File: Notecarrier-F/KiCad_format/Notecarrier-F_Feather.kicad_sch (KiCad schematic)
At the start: 13 parts, among them J7 SM04B-SRSS-TB(LF)(SN), J8 SM04B-SRSS-TB(LF)(SN), SW3 PTS810 SJM 250 SMTR LFS, SW4 CJS-1200TA, SW5 CJS-1200TA, U4 TXS0102DCUR, U6 DGQ2788AEN-T1-GE4

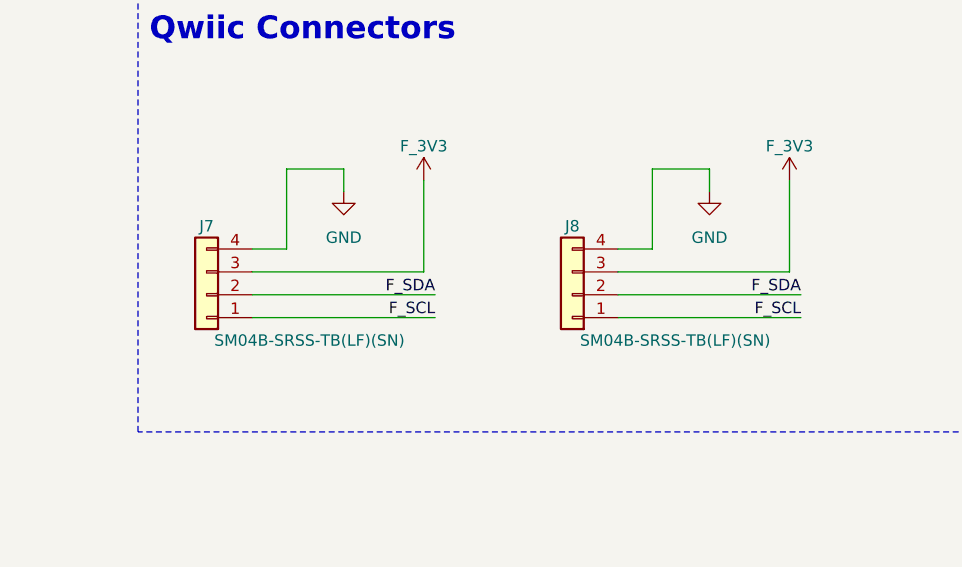
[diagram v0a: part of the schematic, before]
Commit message: Back fill symbol for SM04B-SRSS-TB / BM04B-SRSS-TBT.
Symbol created in the process of porting Notecarrier-A. Creating the symbol wasn’t justified when porting -B and -F, now it exists it’s best to be consistent even though these are SM04B-SRSS-TB (side entry) and the symbol was created for BM04B-SRSS-TBT (top entry).
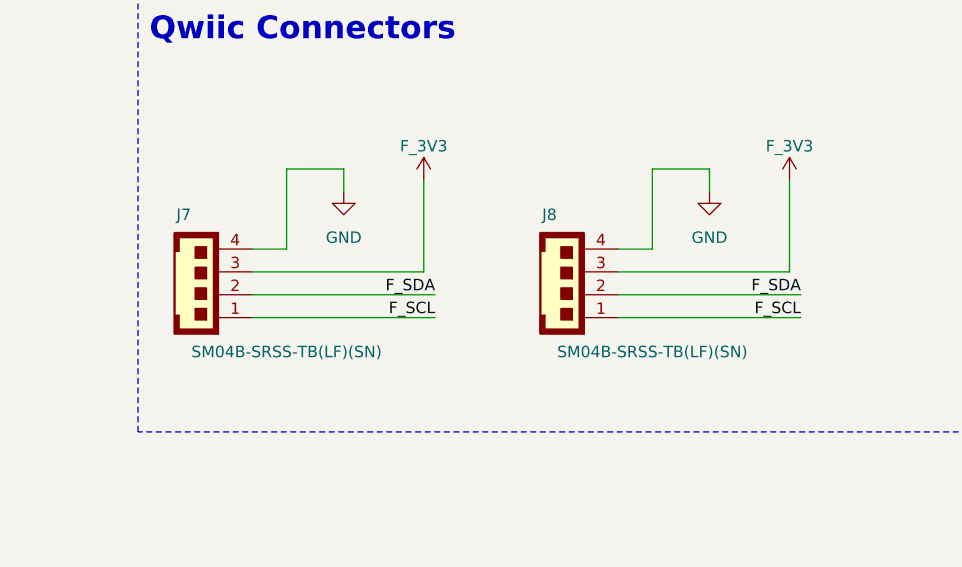
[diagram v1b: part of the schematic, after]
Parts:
- J7, J8: symbol Connector_Generic:Conn_01x04 -> blues-kicad-lib:BM04B-SRSS-TBT
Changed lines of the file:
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@@
     )
   )
-  (symbol (lib_id "Connector_Generic:Conn_01x04") (at 134.62 120.65 180) (unit 1)
-    (in_bom yes) (on_board yes) (dnp no)
-    (property "Reference" "J7" (at 134.62 113.03 0)
-      (effects (font (size 1.27 1.27)))
-    )
-    (property "Value" "SM04B-SRSS-TB(LF)(SN)" (at 146.05 125.73 0)
+  (symbol (lib_id "blues-kicad-lib:BM04B-SRSS-TBT") (at 134.62 120.65 180) (unit 1)
+    (in_bom yes) (on_board yes) (dnp no)
+    (property "Reference" "J7" (at 132.08 111.76 0)
+      (effects (font (size 1.27 1.27)))
+    )
+    (property "Value" "SM04B-SRSS-TB(LF)(SN)" (at 143.51 127 0)
       (effects (font (size 1.27 1.27)))
     )
@@
     )
     (property "Supplier" "Digi-Key" (at 134.62 120.65 0)
+      (effects (font (size 1.27 1.27)) hide)
+    )
+    (property "Critical" "" (at 134.62 120.65 0)
       (effects (font (size 1.27 1.27)) hide)
     )
@@
     )
   )
-  (symbol (lib_id "Connector_Generic:Conn_01x04") (at 175.26 120.65 180) (unit 1)
-    (in_bom yes) (on_board yes) (dnp no)
-    (property "Reference" "J8" (at 175.26 113.03 0)
-      (effects (font (size 1.27 1.27)))
-    )
-    (property "Value" "SM04B-SRSS-TB(LF)(SN)" (at 186.69 125.73 0)
-      (effects (font (size 1.27 1.27)))
-    )
+  (symbol (lib_id "blues-kicad-lib:BM04B-SRSS-TBT") (at 175.26 120.65 180) (unit 1)
+    (in_bom yes) (on_board yes) (dnp no)
+    (property "Reference" "J8" (at 172.72 111.76 0)
+      (effects (font (size 1.27 1.27)))
+    )
+    (property "Value" "SM04B-SRSS-TB(LF)(SN)" (at 184.15 127 0)
+      (effects (font (size 1.27 1.27)))
+    )

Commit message: Start rev B of Notecarrier-F port
Incorporates changes from Altium design files rev 10 (PCB version 1.2).
Block diagram and schematic first pass complete.
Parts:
- removed SW3: PTS810 SJM 250 SMTR LFS, blues-kicad-lib:C&K PTS810, symbol blues-kicad-lib:PTS810-SJM-250-SMTR-LFS
- added C3 (x6): 0.1µF, blues-kicad-lib:CAP 0402_1005, symbol Device:C
- added R3 (x3): 10k, blues-kicad-lib:RES 0402_1005, symbol Device:R
- added R3: 100k, blues-kicad-lib:RES 0402_1005, symbol Device:R
- added U5: DGQ2788AEN-T1-GE4, blues-kicad-lib:QFN40P260X180X60-16N, symbol blues-kicad-lib:DGQ2788AEN-T1-GE4
- added U7: TXS0102DCUR, blues-kicad-lib:SOP50P310X90-8N, symbol blues-kicad-lib:TXS0102DCU
- MOD2: now not fitted
- renumbered J8 to J7, J7 to J8, SW5 to SW3
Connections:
- net EN_F_BAT: now also C3.2, C3.2, R3.2, U5.10 (V+)
- net F_3V3: now also C3.1, R3.2, U7.6 (OE), U7.7 (VCCB); no longer R3.2, R3.2, U4.7 (VCCB)
- net F_B0_SW: now also U5.15 (NO2); no longer U6.1 (NC2)
- net F_BAT: now also R3.2, R3.2, U4.7 (VCCB), C3.1, C3.1, R3.2, R3.2, U7.3 (VCCA)
- net F_EN: now also SW3.3 (A)
- net F_NRST_SW: now also U5.11 (NO1); no longer U6.13 (NC1)
- net F_RX_SW: now also U5.7 (NO4); no longer U6.9 (NC4)
- net F_SCL: now also U7.4 (A2); no longer J7.1, J8.1
- net F_SDA: now also U7.5 (A1); no longer J7.2, J8.2
- net F_TX_SW: now also U5.3 (NO3); no longer U6.5 (NC3)
- net GND: now also C3.1, C3.1, C3.2, C3.2, C3.2, C3.2, R3.1, U5.2 (GND), U7.2 (GND)
- net N_VIO: now also C3.1; no longer SW3.3 (A)
- new net: U5.12 (COM1), U6.13 (NC1)
- new net: U5.16 (COM2), U6.1 (NC2)
- new net: U5.4 (COM3), U6.5 (NC3)
- new net: U5.8 (COM4), U6.9 (NC4)
- new net ALT_DFU_ACTIVE: R3.1, U5.14 (IN1-2), U5.6 (IN3-4)
- new net ALT_DFU_BOOT: U5.1 (NC2)
- new net ALT_DFU_RESET: U5.13 (NC1)
- new net ALT_DFU_RX: U5.5 (NC3)
- new net ALT_DFU_TX: U5.9 (NC4)
- new net SW_SCL: J7.1, J8.1, R3.1, U7.1 (B2)
- new net SW_SDA: J7.2, J8.2, R3.1, U7.8 (B1)
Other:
- note added: "DFU Enable"
- note added: "Logic Level Shifter"
- note added: "QWIIC Connectors"
- note added: "See note on Notecard sheet."
- note added: "[DFU]"
- note added: "[NORMAL]"
- note added: "[N_ATTN]"
- note added: "[ON]"
- note removed: "ATTN MODE ENABLE"
- note removed: "DFU ENABLE"
- note removed: "FEATHER"
- note removed: "FLICK SWITCH TOWARDS THE TEXT "ON" TO ENABLE OUTBOARD DFU"
- note removed: "Feather PWR flicked towards the text ON means "ATTN MODE" IS OFF"
- note removed: "I2C Level Shifter"
- note removed: "NOTECARD OR IO HEADER"
- note removed: "ON"
- note removed: "Qwiic Connectors"
- note removed: "SWITCHED"
- note removed: "Several of the net labels on this sheet need to be common with other sheets. In the original Altium source files, this was achieved for some labels by adding Off-Sheet Connectors to the nets. But any others (inadvertently perhaps) rely on promoting all net labels to global using the "Net Identifier Scope" setting. This renders the original Off Sheet Connectors redundant. To avoid losing that dist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"
- note removed: "TRUTH TABLE: IN1-2, IN3-4 LOGIC 0 = NC is TRUE/HIGH DFU=N LOGIC 1 = NO is TRUE/HIGH DFU=Y"
- note removed: "USER"
- moved on the sheet: J7, J8, MODL1, MODR1, R3, SW3, SW4, TP1, U4, U6

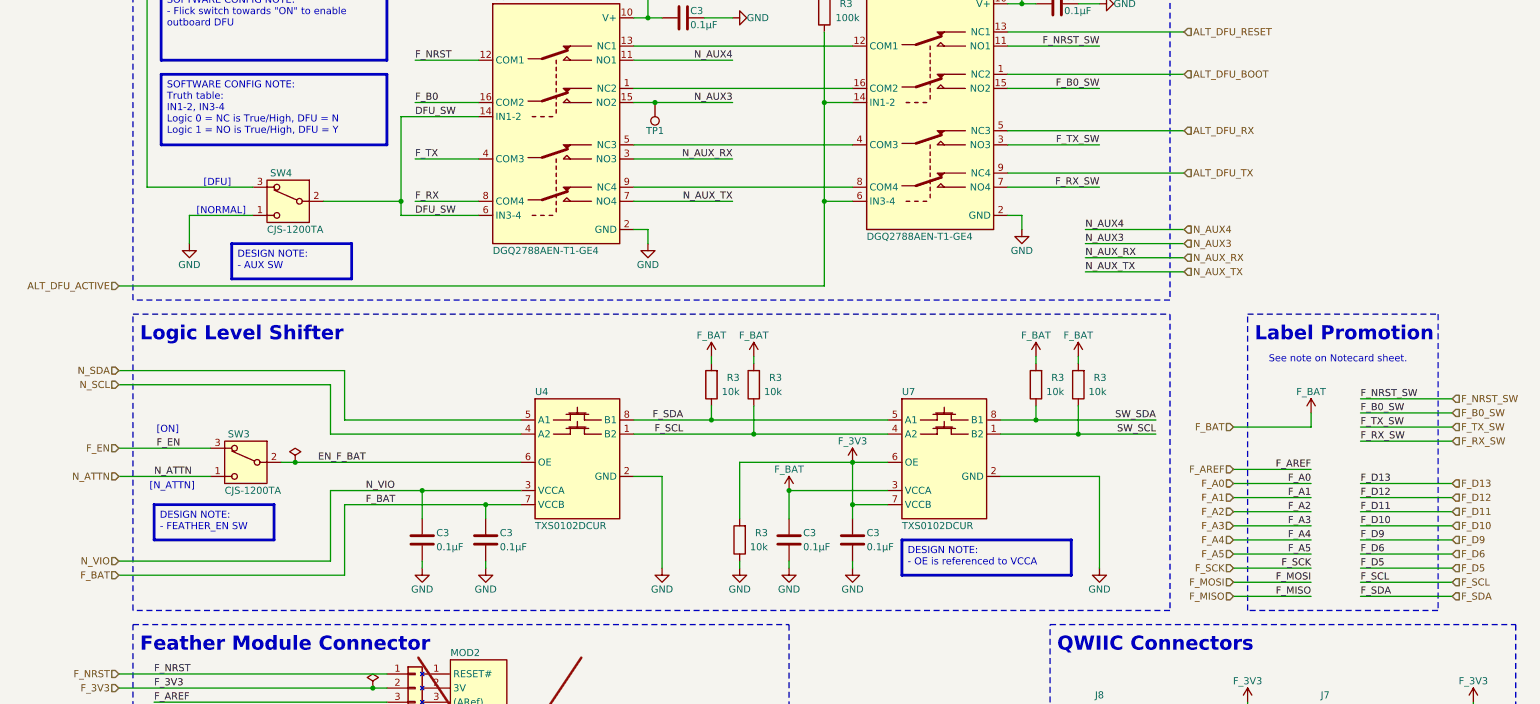
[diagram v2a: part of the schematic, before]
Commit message: Complete first pass PCB rev B.
See README for details. Ready to start Validation.
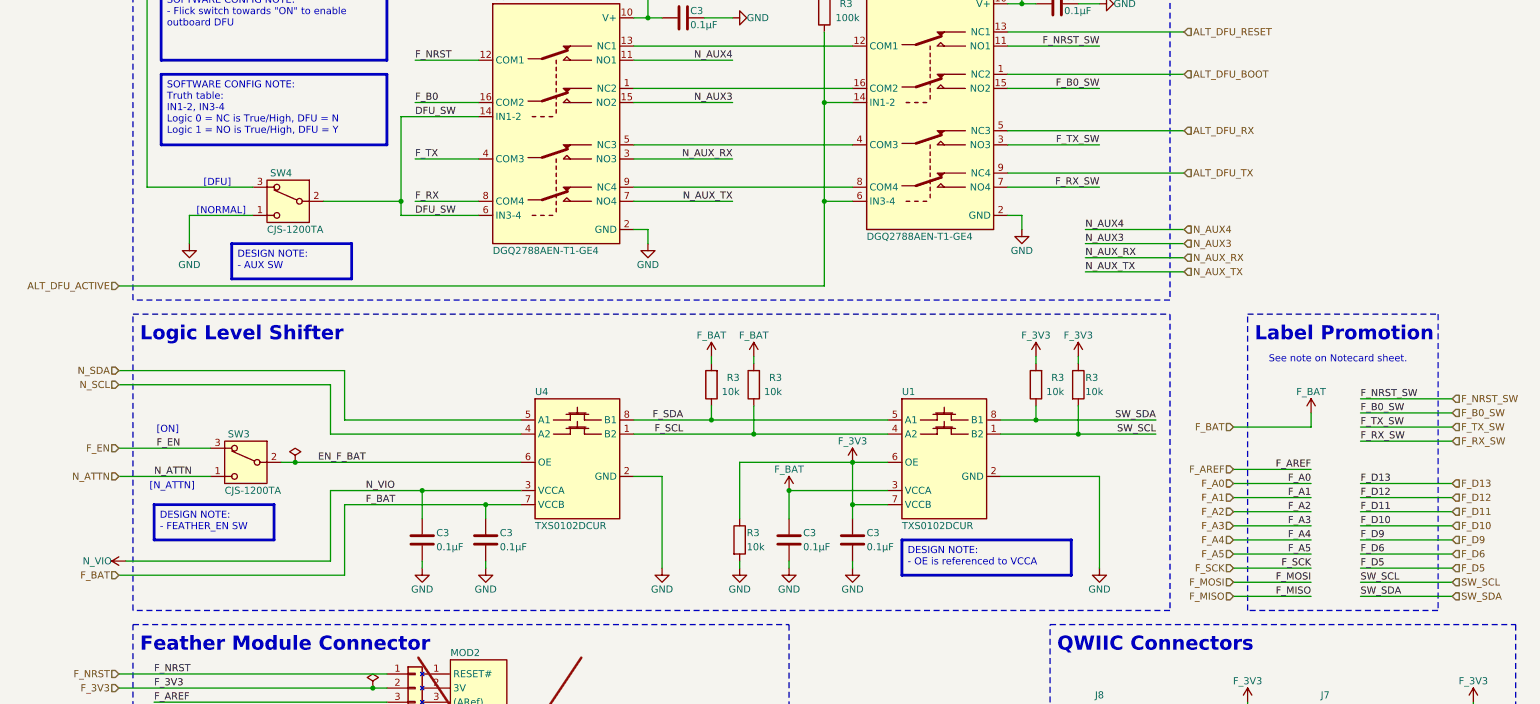
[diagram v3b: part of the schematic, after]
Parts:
- removed TP1: TESTPAD, blues-kicad-lib:TESTPAD_127, symbol Connector:TestPoint
- C3: footprint blues-kicad-lib:CAP 0402_1005 -> blues-kicad-lib:C-0402_Fv1.2; Datasheet 2 (none) -> http://datasheet.octopart.com/CL05B104KO5NNNC-Samsung-Elect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; Datasheet 3 (none) -> https://datasheet.octopart.com/GRM155R71C104KA88D-Murata-da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; Design Description (none) -> Capacitor ceramic 100n ±10% X7R 16V 0402; Design MPN (none) -> N/A; Design Manufacturer (none) -> N/A; Design Order Code (none) -> 490-3261-1-ND; Design Supplier (none) -> Digi-Key; MPN (none) -> CC0402KRX7R7BB104; MPN 2 (none) -> CL05B104KO5NNNC; MPN 3 (none) -> GRM155R71C104KA88D; Manufacturer Samsung -> Yageo; Manufacturer 2 (none) -> Samsung; Manufacturer 3 (none) -> Murata; Mfr Description (none) -> 0402 0.1 uF 16 V ±10 % Tolerance X7R SMT Multilayer Ceramic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; Mfr Description 2 (none) -> Ceramic capacitor SMD-0402 100nF /16V X7R# K +-10%, Samsung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; Mfr Description 3 (none) -> Multilayer Ceramic Capacitor, 0.1 uF, 16 V, ± 10%, X7R, 040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; Order Code 187-CL05B104KO5NNNC -> (none); Part Number CL05B104KO5NNNC -> (none); Supplier Farnell -> (none)
- J7, J8: footprint blues-kicad-lib:JST SM04B-SRSS-TB -> blues-kicad-lib:JST SM04B-SRSS-TB_Fv1.2; Design Description (none) -> CONN HEADER SH 4POS SIDE 1MM TIN; Design MPN (none) -> SM04B-SRSS-TB(LF)(SN); Design Manufacturer (none) -> JST Sales America Inc.; Design Order Code (none) -> 455-1804-1-ND; Design Supplier (none) -> Digi-Key; MPN (none) -> SM04B-SRSS-TB(LF)(SN); Mfr Description (none) -> Connector Header, Side Entry, SR Series, 4 Position, 1.00mm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; Order Code 455-1804-1-ND -> (none); Part Number SM04B-SRSS-TB-LFSN -> (none); Supplier Digi-Key -> (none)
- MOD2: footprint blues-kicad-lib:BLUES_WIRELESS_SWAN_2-54_HEADERS -> blues-kicad-lib:BLUES_WIRELESS_SWAN_2-54_HEADERS_Fv1.2
- MODL1: footprint blues-kicad-lib:16PIN_254MM -> blues-kicad-lib:16PIN_254MM_Fv1.2; Datasheet 2 (none) -> http://www.4uconnector.com/online/object/4udrawing/00542.pdf; Design Description (none) -> Socket 16-Pin, 0.100 in; Design MPN (none) -> CES-116-01-L-S; Design Manufacturer (none) -> Samtec Inc.; Design Order Code (none) -> CES-116-01-L-S-ND; Design Supplier (none) -> Digi-Key; MPN (none) -> PPTC161LFBN-RC; MPN 2 (none) -> 00542; Manufacturer 4UCONN -> Sullins; Manufacturer 2 (none) -> 4UCON; Mfr Description (none) -> Sullins Connector Solutions PPTC161LFBN-RC / Conn Header Fe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; Order Code 00542 -> (none); Part Number 00542 -> (none)
- MODR1: footprint blues-kicad-lib:12PIN_254MM -> blues-kicad-lib:12PIN_254MM_Fv1.2; Datasheet 2 (none) -> http://www.4uconnector.com/online/object/4udrawing/00536.pdf; Design Description (none) -> Socket 12-Pin, 0.100 in; Design MPN (none) -> CES-112-01-L-S; Design Manufacturer (none) -> Samtec Inc.; Design Order Code (none) -> 612-CES-112-01-L-S-ND; Design Supplier (none) -> Digi-Key; MPN (none) -> PPTC121LFBN-RC; MPN 2 (none) -> 00536; Manufacturer 4UCONN -> Sullins; Manufacturer 2 (none) -> 4UCON; Mfr Description (none) -> Conn Socket Strip F 12 POS 2.54mm Solder ST Thru-Hole; Order Code 00536 -> (none); Part Number 00536 -> (none)
- R3: footprint blues-kicad-lib:RES 0402_1005 -> blues-kicad-lib:R-0402_Fv1.2; Datasheet 2 (none) -> http://datasheet.octopart.com/RC0402FR-0710KL-Yageo-datashe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; Datasheet 3 (none) -> https://datasheet.octopart.com/ERJ-2RKF1002X-Panasonic-data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; Design Description (none) -> Resistor 10k ±1% 0402; Design MPN (none) -> N/A; Design Manufacturer (none) -> N/A; Design Order Code (none) -> 311-10.0KLRCT-ND; Design Supplier (none) -> Digi-Key; MPN (none) -> RC1005F103CS; MPN 2 (none) -> RC0402FR-0710KL; MPN 3 (none) -> ERJ-2RKF1002X; Manufacturer 2 (none) -> Yageo; Manufacturer 3 (none) -> Panasonic; Mfr Description (none) -> Res Thick Film 0402 10K Ohm 1% 1/16W ±100ppm/°C Molded SMD 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; Mfr Description 2 (none) -> Res General Purpose Thick Film 0402 10K Ohm 1% 1/16W ±100pp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; Mfr Description 3 (none) -> Res Thick Film 0402 10K Ohm 1% 1/10W ±100ppm/°C Molded SMD 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; Order Code 1276-3431-2-ND -> (none); Part Number RC1005F103CS -> (none); Supplier Digi-Key -> (none)
- R3: footprint blues-kicad-lib:RES 0402_1005 -> blues-kicad-lib:R-0402_Fv1.2; Design Description (none) -> Resistor 100k ±1% 0402; Design MPN (none) -> N/A; Design Manufacturer (none) -> N/A; Design Order Code (none) -> RHM100CDCT-ND; Design Supplier (none) -> Digi-Key; MPN (none) -> RC0402FR-07100KL; Manufacturer Samsung -> Yageo; Mfr Description (none) -> Res General Purpose Thick Film 0402 100K Ohm 1% 1/16W ±100p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; Order Code 1276-3431-2-ND -> (none); Part Number RC1005F103CS -> (none); Supplier Digi-Key -> (none)
- SW3, SW4: footprint blues-kicad-lib:SW_CJS-1200TA -> blues-kicad-lib:SW_CJS-1200TA_Fv1.2; Datasheet 2 (none) -> https://datasheet.octopart.com/CJS-1200TA1-Nidec-Copal-data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; Design Description (none) -> Switch Slide N.O./N.C. SPDT Raised Slide 0.1A 24VDC J-Hook 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; Design MPN (none) -> CJS-1200TA; Design Manufacturer (none) -> Nidec Copal; Design Order Code (none) -> 563-1021-6-ND; Design Supplier (none) -> Digi-Key; MPN (none) -> CJS-1200TA; MPN 2 (none) -> CJS-1200TA1; MPN 3 (none) -> CJS-1200TA2; Manufacturer 2 (none) -> Nidec Copal; Manufacturer 3 (none) -> Nidec Copal; Mfr Description (none) -> Switch Slide N.O./N.C. SPDT Raised Slide 0.1A 24VDC J-Hook 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; Mfr Description 2 (none) -> Switch Slide DIP SPDT 100MA 6V; Mfr Description 3 (none) -> SPDT, ON-ON Slide, 100mA @ 6V DC J-Hook SMD Terminals, T&R 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; Order Code 563-1021-6-ND -> (none); Part Number CJS-1200TA -> (none); Supplier Digi-Key -> (none)
- U1: renamed from U7; footprint blues-kicad-lib:SOP50P310X90-8N -> blues-kicad-lib:SOP50P310X90-8N_Fv1.2; Design Description (none) -> 2-Bit Bidirectional Voltage-Level Shifter for Open-Drain an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; Design MPN (none) -> TXS0102DCUR; Design Manufacturer (none) -> Texas Instruments; Design Order Code (none) -> 296-21931-6-ND; Design Supplier (none) -> Digi-Key; MPN (none) -> TXS0102DCUR; Mfr Description (none) -> 2-Bit Bidirectional Voltage-Level Shifter for Open-Drain an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; Order Code 296-21931-6-ND -> (none); Part Number TXS0102DCUR -> (none); Supplier Digi-Key -> (none)
- U4: footprint blues-kicad-lib:SOP50P310X90-8N -> blues-kicad-lib:SOP50P310X90-8N_Fv1.2; Design Description (none) -> 2-Bit Bidirectional Voltage-Level Shifter for Open-Drain an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; Design MPN (none) -> TXS0102DCUR; Design Manufacturer (none) -> Texas Instruments; Design Order Code (none) -> 296-21931-6-ND; Design Supplier (none) -> Digi-Key; MPN (none) -> TXS0102DCUR; Mfr Description (none) -> 2-Bit Bidirectional Voltage-Level Shifter for Open-Drain an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; Order Code 296-21931-6-ND -> (none); Part Number TXS0102DCUR -> (none); Supplier Digi-Key -> (none)
- U5, U6: footprint blues-kicad-lib:QFN40P260X180X60-16N -> blues-kicad-lib:QFN40P260X180X60-16N_Fv1.2; Design Description (none) -> Analog Switch Quad SPDT Automotive 16-Pin Mini-QFN T/R; Design MPN (none) -> DGQ2788AEN-T1-GE4; Design Manufacturer (none) -> Vishay; Design Order Code (none) -> DGQ2788AEN-T1-GE4CT-ND; Design Supplier (none) -> Digi-Key; MPN (none) -> DGQ2788AEN-T1-GE4; Mfr Description (none) -> Analog Switch Quad SPDT Automotive 16-Pin Mini-QFN T/R; Order Code DGQ2788AEN-T1-GE4 -> (none); Part Number DGQ2788AEN-T1-GE4 -> (none); Supplier Arrow Electronics -> (none)
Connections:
- net F_3V3: now also R3.1, R3.1, R3.2; no longer R3.2
- net F_BAT: no longer R3.2, R3.2
- net GND: now also R3.2; no longer R3.1
- net SW_SCL: now also R3.2; no longer R3.1
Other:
- moved on the sheet: R3

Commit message: Apply minor corrections from BOM validation.
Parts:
- MODL1: value Conn_01x16 -> CES-116-01-L-S; Mfr Description 2 (none) -> 2.54 FEMALE HEADER DIP 180° HEIGHT=8.5MM 1X16PIN GOLD FLASH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
- MODR1: value Conn_01x12 -> CES-112-01-L-S; Mfr Description 2 (none) -> 2.54 FEMALE HEADER DIP 180° HEIGHT=8.5MM 1X12PIN GOLD FLASH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
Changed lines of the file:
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@@
       (effects (font (size 1.27 1.27)))
     )
-    (property "Value" "Conn_01x12" (at 114.3 157.48 0)
+    (property "Value" "CES-112-01-L-S" (at 114.3 157.48 0)
       (effects (font (size 1.27 1.27)) hide)
     )
@@
       (effects (font (size 1.27 1.27)) hide)
     )
-    (property "Mfr Description 2" "" (at 114.3 172.72 0)
+    (property "Mfr Description 2" "2.54 FEMALE HEADER DIP 180° HEIGHT=8.5MM 1X12PIN GOLD FLASH WITHSTAND HIGH TEMPERATURE MOQ=1000PC RoHS" (at 114.3 172.72 0)
       (effects (font (size 1.27 1.27)) hide)
     )
@@
       (effects (font (size 1.27 1.27)) (justify left))
     )
-    (property "Value" "Conn_01x16" (at 77.47 191.77 0)
+    (property "Value" "CES-116-01-L-S" (at 77.47 191.77 0)
       (effects (font (size 1.27 1.27)) (justify left) hide)
     )
@@
       (effects (font (size 1.27 1.27)) hide)
     )
-    (property "Mfr Description 2" "" (at 83.82 167.64 0)
-      (effects (font (size 1.27 1.27)) hide)
-    )
+    (property "Mfr Description 2" "2.54 FEMALE HEADER DIP 180° HEIGHT=8.5MM 1X16PIN GOLD FLASH WITHSTAND HIGH TEMPERATURE TRAY MOQ=1000PC RoHS" (at 83.82 167.64 0)
+      (effects (font (size 1.27 1.27)) hide)
+    )
